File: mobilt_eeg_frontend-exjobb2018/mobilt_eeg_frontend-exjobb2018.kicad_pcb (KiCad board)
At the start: 2 copper layers, 95 x 90.5 mm, 126 parts, among them J1 Conn_02x04_Odd_Even, J11 Conn_01x02, J2 Conn_02x20_Odd_Even, J3 Conn_02x04_Odd_Even, J5 Data Header, J8 Conn_01x08, J9 Conn_01x04, P1 Conn_02x20_Odd_Even, SW1 SW_DIP_x01, SW2 SW_DIP_x01, U1 ADS1299-4PAG, U2 TPS60403DBVR, U3 TPS72325DBVT, U4 TPS73225DBVT, U5 TPS73233DBVT, U6 CAT24C256, U7 arduino_pro_mini_3V3_sparkfun, X1 X1G0044810050_SG7050CAN_2.048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

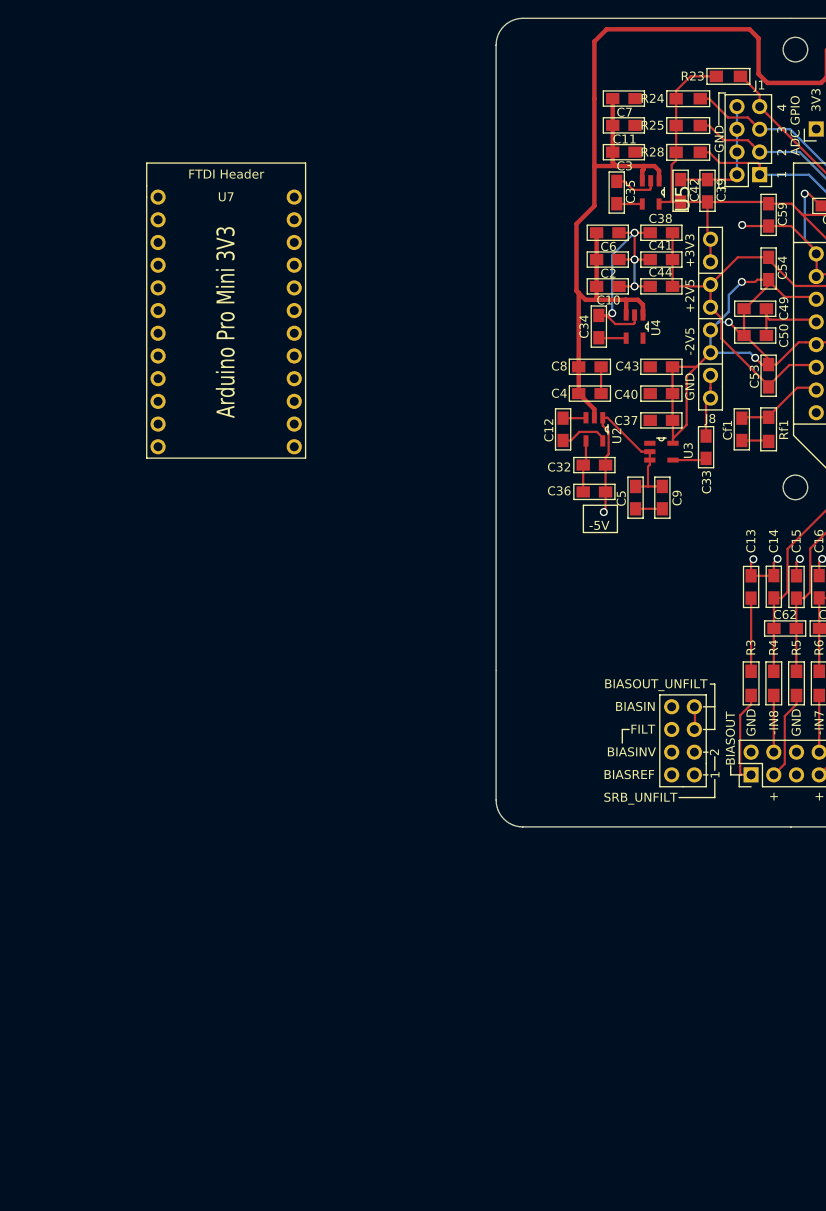
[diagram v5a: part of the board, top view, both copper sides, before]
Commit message: starting to shift things around in preparation for grid alignment
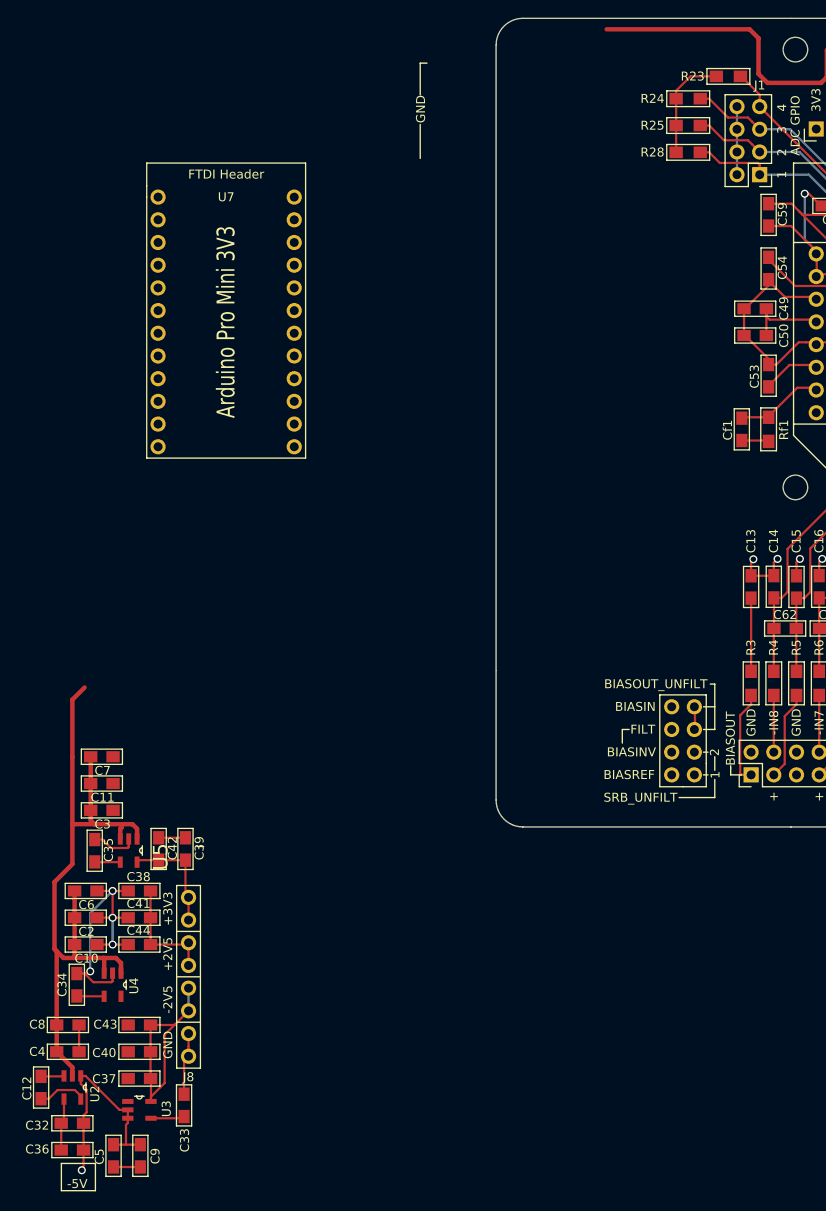
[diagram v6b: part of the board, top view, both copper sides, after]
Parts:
- moved C39 94.0 mm to (135.2, 187.0)
- moved C42 94.0 mm to (132.2, 187.0)
- moved C9 94.0 mm to (130.2, 221.3)
- moved C10 94.0 mm to (124.1, 197.7)
- moved C12 94.0 mm to (119.1, 213.7)
- moved C2 94.0 mm to (124.1, 194.7)
- moved C32 94.0 mm to (122.6, 217.7)
- moved C34 94.0 mm to (123.1, 202.2)
- moved C35 94.0 mm to (125.1, 187.2)
- moved C36 94.0 mm to (122.6, 220.7)
- moved C4 94.0 mm to (122.1, 209.7)
- moved C5 94.0 mm to (127.2, 221.3)
- moved C6 94.0 mm to (124.1, 191.7)
- moved C8 94.0 mm to (122.1, 206.7)
- moved U2 94.0 mm to (122.6, 213.7)
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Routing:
- net AVSS: track 165.7 -> 145.2 mm, vias 4 -> 1
- net AVDD: track 69.5 -> 50.0 mm
- net DVDD: track 100.6 -> 87.0 mm
- net AGND: track 238.2 -> 231.6 mm, vias 30 -> 29
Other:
- board text added: "Notes All 2.54mm headers conform to 2.54mm grid with origo on Pi header pin 1. All SMD components conform to 1mm grid with origo on Pi header pin 1. Edge Cuts conform to 0.5mm grid with DEFAULT origo (hotkey Z)."
- board text removed: "Notes All 2.54mm headers conform to 2.54mm grid with origo on Pi header pin 1. All SMD components conform to 1mm grid with origo on Pi header pin 1."

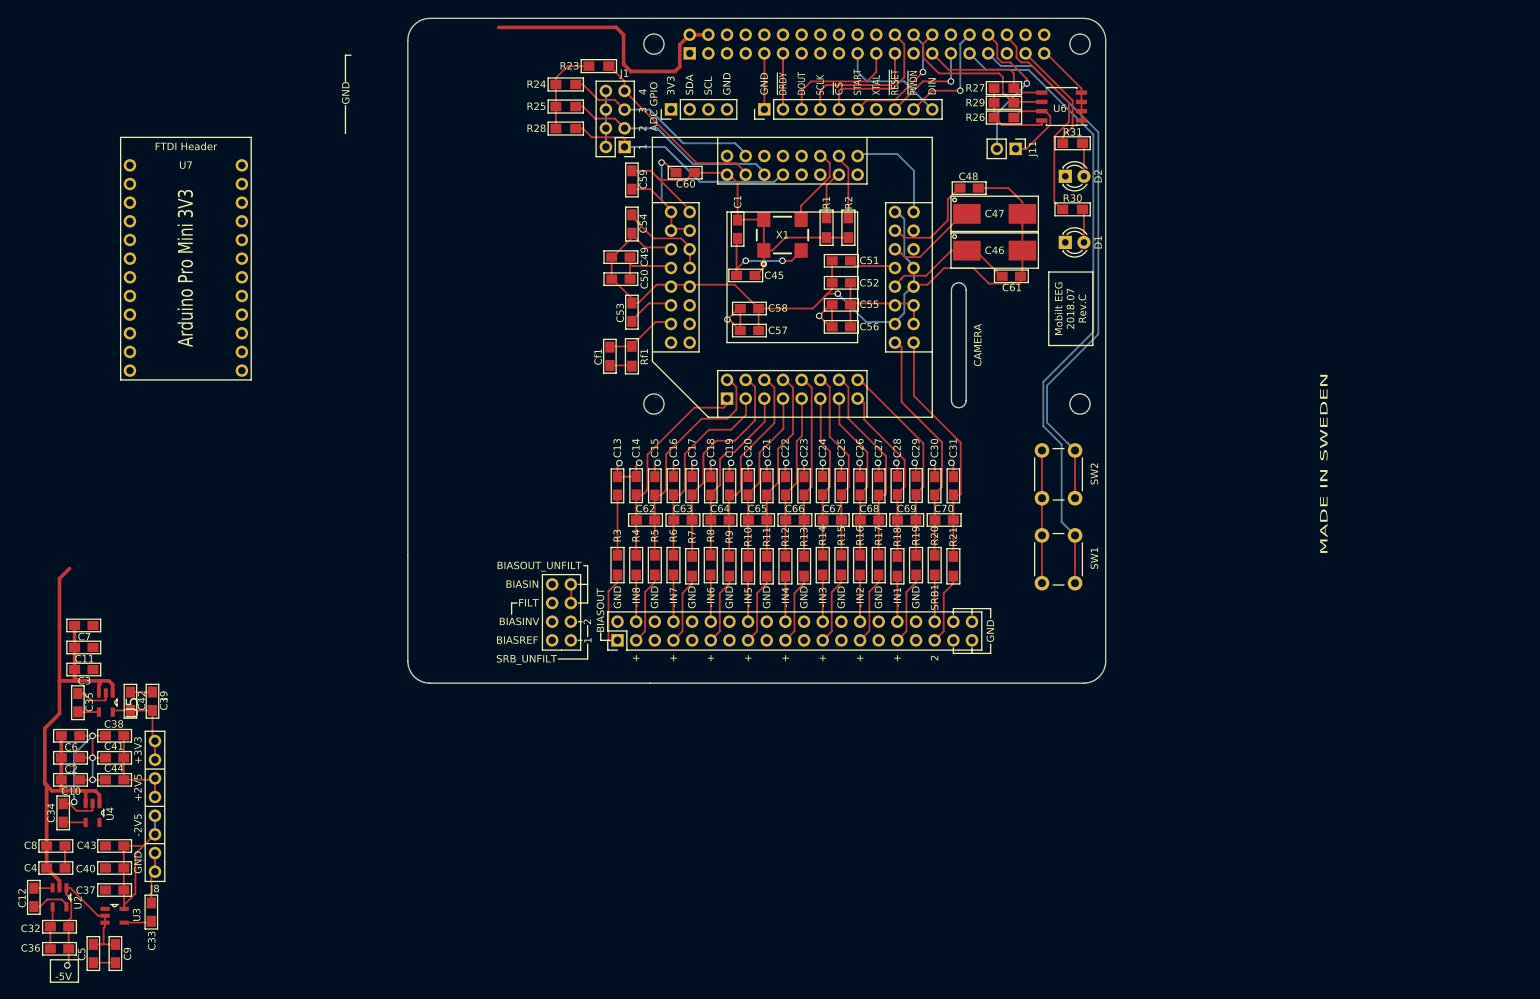
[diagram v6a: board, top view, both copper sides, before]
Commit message: Aligned a few things to new grid system. Tested arduino footprint suitability.
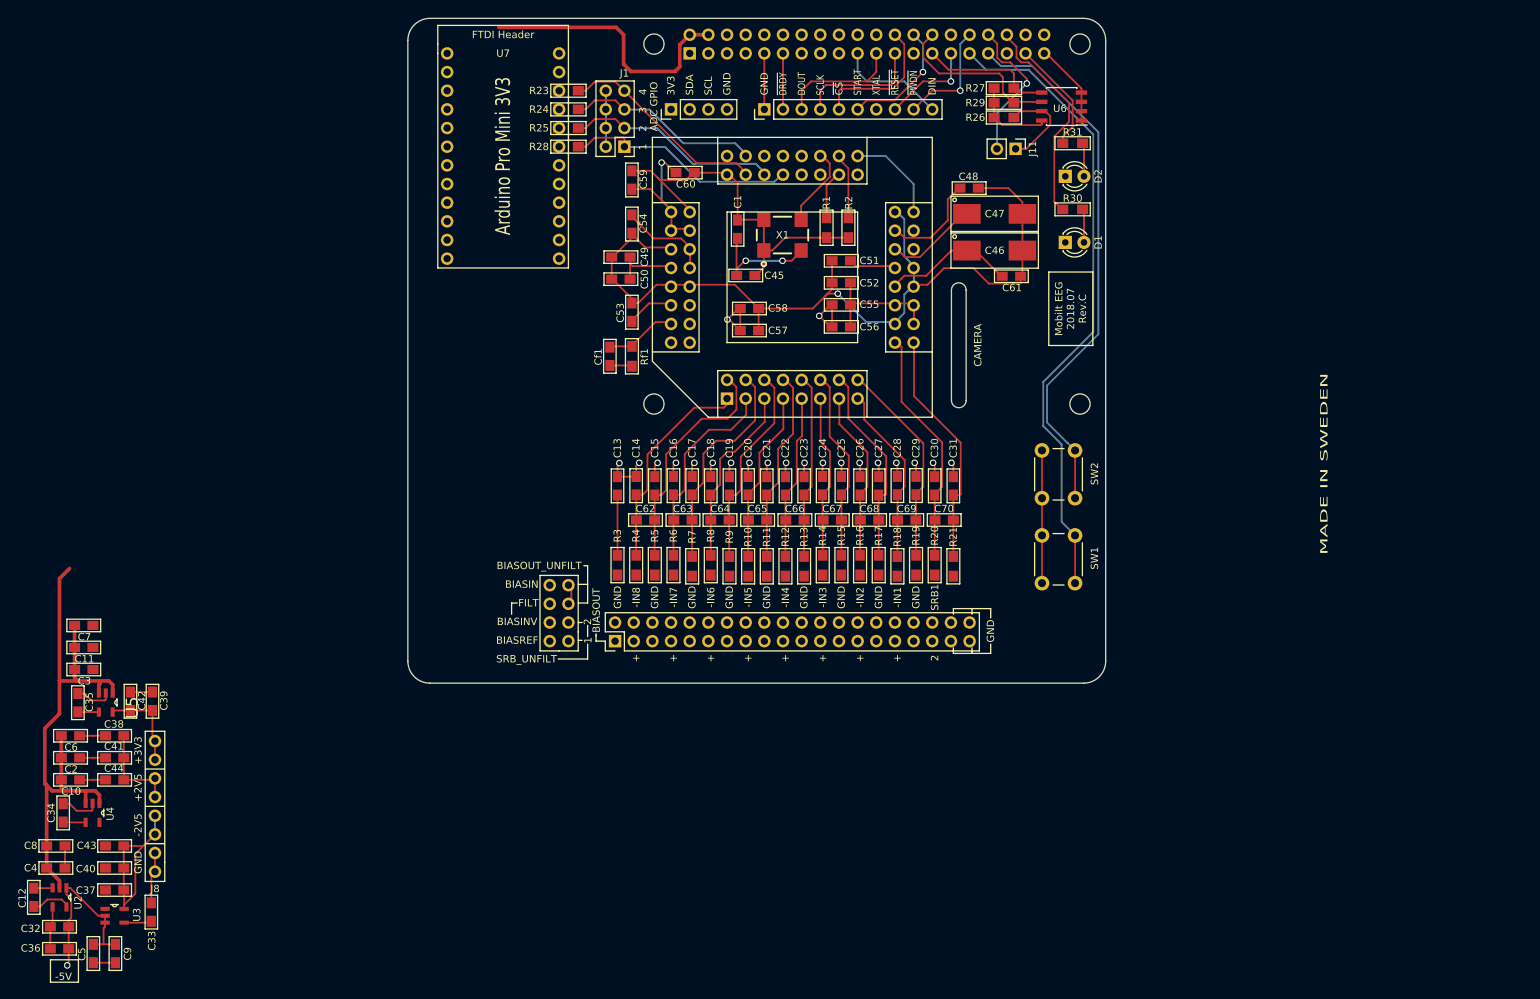
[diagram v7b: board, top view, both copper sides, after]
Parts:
- moved U7 45.8 mm to (175.3, 98.8)
- moved R23 5.33 mm to (191.9, 103.8)
- moved R24 3.41 mm to (191.9, 106.4)
- moved R25 2.95 mm to (191.9, 108.9)
- moved R28 2.50 mm to (191.9, 111.5)
- moved J2 0.35 mm to (198.2, 178.8)
- moved J3 0.35 mm to (191.9, 178.8)
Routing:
- net AGND: track 231.6 -> 213.1 mm, vias 29 -> 25
- net DVDD: track 87.0 -> 75.0 mm
- net /BIASOUT_FILTERED: track 10.5 -> 0.00 mm
- net Net-(J2-Pad31): track 9.94 -> 0.00 mm
- net Net-(J2-Pad23): track 9.94 -> 0.00 mm
- net Net-(J2-Pad3): track 9.94 -> 0.00 mm
- net Net-(J2-Pad27): track 9.94 -> 0.00 mm
- net Net-(J2-Pad11): track 9.90 -> 0.00 mm
- net Net-(J2-Pad15): track 9.78 -> 0.00 mm
- net Net-(J2-Pad7): track 9.78 -> 0.00 mm
- net Net-(J2-Pad19): track 9.78 -> 0.00 mm
- net /SRB2_FILT: track 9.78 -> 0.00 mm
- net Net-(J2-Pad8): track 6.35 -> 0.00 mm
- net Net-(J2-Pad4): track 6.35 -> 0.00 mm
- net Net-(J2-Pad28): track 6.35 -> 0.00 mm
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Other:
- outline, holes or cut-outs redrawn
- board text added: "Notes All 2.54mm headers conform to 2.54mm grid with origo on Pi header pin 1. All SMD components conform to 1mm grid with origo on Pi header pin 1. Edge Cuts conform to 0.5mm grid with origo SNAPPED TO EXISTING LINES."
- board text removed: "Notes All 2.54mm headers conform to 2.54mm grid with origo on Pi header pin 1. All SMD components conform to 1mm grid with origo on Pi header pin 1. Edge Cuts conform to 0.5mm grid with DEFAULT origo (hotkey Z)."

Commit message: savea
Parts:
- moved U7 20.0 mm to (175.4, 118.8)
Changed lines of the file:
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@@
-(kicad_pcb (version 20171130) (host pcbnew "(6.0.0-rc1-dev-195-gf5e23e4f1)")
+(kicad_pcb (version 20171130) (host pcbnew "(6.0.0-rc1-dev)")
   (general
     (thickness 1.6)
@@
     (zone_45_only no)
     (trace_min 0.15)
+    (segment_width 0.15)
+    (edge_width 0.1)
     (via_size 0.9)
     (via_drill 0.6)
@@
     (uvia_min_size 0.5)
     (uvia_min_drill 0.1)
-    (edge_width 0.1)
-    (segment_width 0.15)
     (pcb_text_width 0.3)
     (pcb_text_size 1 1)
@@
     (aux_axis_origin 200 150)
     (grid_origin 208.37 98.77)
-    (visible_elements 7FFFF7FF)
+    (visible_elements 7FFFFFFF)
     (pcbplotparams
       (layerselection 0x01030_ffffffff)
@@
     (uvia_dia 0.5)
     (uvia_drill 0.1)
+    (diff_pair_gap 0.25)
     (diff_pair_width 0.25)
-    (diff_pair_gap 0.25)
     (add_net /BIASIN)
     (add_net /BIASINV)
@@
     (uvia_dia 0.5)
     (uvia_drill 0.1)
+    (diff_pair_gap 0.25)
     (diff_pair_width 0.25)
-    (diff_pair_gap 0.25)
     (add_net +5V)
     (add_net /+3V3_Pi)
@@
   )
   (module prj_lib_fp:arduino_pro_mini_3V3_sparkfun (layer F.Cu)
-    (at 175.35 98.77)
+    (at 175.37 118.77)
     (fp_text reference U7 (at 7.62 0) (layer F.SilkS)
       (effects (font (size 1 1) (thickness 0.15)))
